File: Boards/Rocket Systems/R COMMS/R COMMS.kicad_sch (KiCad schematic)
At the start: 67 parts, among them IC1 NSVT30010MXV6T1G, IC2 NSVT30010MXV6T1G, J2 22285061, J4 MEM2061-01-188-00-A_REVA, J5 SMA_CONNECTOR, J6 SMA_CONNECTOR, J7 SMA_CONNECTOR, J8 1190297, SW1 D2F-01-D, U3 SX1280IMLTRT, U4 NRF21540-QDAA-R, U6 MAX485CSA+T, U7 MCP9808T-E/MC, U9 CD-PA1616

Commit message: Update R Comms board
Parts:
- R15, R17: value 10K -> 10k
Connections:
- net +3.3V: now also R15.1; no longer R15.2
- net NRF21540 SPI ~{CS}: no longer IC2.2 (B2)
- net RS_ENABLE: now also IC2.5 (B1)
- net SX1280 SPI ~{CS}: no longer IC2.5 (B1)
- net TEMP ALERT: now also IC2.2 (B2)
- net GPS I2C SCL renamed SDL I2C
- net GPS I2C SDA renamed SDA I2C
- net SDA I2C: now also R15.2; no longer R15.1
- net GPS UART RX: no longer names the net of U9.10 (RX0)
- net GPS UART TX: no longer names the net of U9.9 (TX0)
- no-connect marks 4 -> 6
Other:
- sheet RP2040 ports: added GP13/SPI1 ~{CS}, GPIO12; removed GP12/I2C0 SDA, GP13/I2C0 SCL
- note added: "I2C for GPS & Temp Sensor"
- moved on the sheet: CR3, CR5, CR6, IC2, J2, R22, R25

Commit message: Communication boards update
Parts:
- removed J2: 22285061, CONN Male Header:CONN_SD-42375-001_M320_06_MOL, symbol 2025-01-27_18-08-00:22285061
- added J2: 22022065, CONN_SA-4455_06_TE_MOL, symbol CONN_SA-4455_06_TE_MOL:22022065
- U3: footprint SX1280:QFN24_4X4_SEM -> QFN24_4X4_SEM
- U4: footprint RF FEM:QFN16_4X4_NOR -> QFN16_4X4_NOR
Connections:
- net NRF21540 SPI MISO is gone; now on net RADIO SPI MISO: U4.14 (MISO)
- net NRF21540 SPI MOSI is gone; now on net RADIO SPI MOSI: U4.13 (MOSI)
- net NRF21540 SPI SCK is gone; now on net RADIO SPI SCK: U4.12 (SCK)
- net SX1280 SPI MISO is gone; now on net RADIO SPI MISO: U3.16 (MISO_TX)
- net SX1280 SPI MOSI is gone; now on net RADIO SPI MOSI: U3.17 (MOSI_RX)
- net SX1280 SPI SCK is gone; now on net RADIO SPI SCK: U3.18 (SCK_RTSN)
- net TEMP SDA I2C is gone; now on net SDA I2C: R21.2, U7.1 (SDA)
- net TEMP SDL I2C is gone; now on net SDL I2C: R20.2, U7.2 (SCL)
- net GND: now also J2.6
- net OBC UART CTS: now also J2.4
- net OBC UART RTS: now also J2.5
- net OBC UART RX: now also J2.3
- net OBC UART TX: now also J2.2
- net V_IN: now also J2.1
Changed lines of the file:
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@@
 		)
 	)
-	(label "NRF21540 SPI MISO"
+	(label "RADIO SPI MISO"
 		(at 218.44 238.76 0)
 		(effects
@@
 		)
 	)
-	(label "NRF21540 SPI SCK"
+	(label "RADIO SPI SCK"
 		(at 218.44 233.68 0)
 		(effects
@@
 		)
 	)
-	(label "SX1280 SPI SCK"
+	(label "RADIO SPI SCK"
 		(at 168.91 236.22 180)
 		(effects
@@
 		)
 	)
-	(label "NRF21540 SPI MOSI"
+	(label "RADIO SPI MOSI"
 		(at 218.44 236.22 0)
 		(effects
@@
 		)
 	)
-	(label "TEMP SDA I2C"
+	(label "SDA I2C"
 		(at 21.59 154.305 0)
 		(effects
@@
 		)
 	)
-	(label "TEMP SDL I2C"
+	(label "SDL I2C"
 		(at 21.59 156.845 0)
 		(effects
@@
 		)
 	)
-	(label "SX1280 SPI MISO"
+	(label "RADIO SPI MISO"
 		(at 168.91 241.3 180)
 		(effects
@@
 		)
 	)
-	(label "SX1280 SPI MOSI"
+	(label "RADIO SPI MOSI"
 		(at 168.91 238.76 180)
 		(effects
@@
 	)
 	(symbol
-		(lib_id "2025-01-27_18-08-00:22285061")
-		(at 33.655 58.42 180)
-		(unit 1)
-		(exclude_from_sim no)
-		(in_bom yes)
-		(on_board yes)
-		(dnp no)
-		(fields_autoplaced yes)
-		(property "Reference" "J2"
-			(at 24.765 38.1 0)
-			(effects
-				(font
-					(size 1.524 1.524)
-				)
-			)
-		)
-		(property "Value" "22285061"
-			(at 24.765 40.64 0)
-			(effects
-				(font
-					(size 1.524 1.524)
-				)
-			)
-		)
-		(property "Footprint" "CONN Male Header:CONN_SD-42375-001_M320_06_MOL"
-			(at 33.655 58.42 0)
-			(effects
-				(font
-					(size 1.27 1.27)
-					(italic yes)
-				)
-				(hide yes)
-			)
-		)
-		(property "Datasheet" "22285061"
-			(at 33.655 58.42 0)
-			(effects
-				(font
-					(size 1.27 1.27)
-					(italic yes)
-				)
-				(hide yes)
-			)
-		)
-		(property "Description" ""
-			(at 33.655 58.42 0)
-			(effects
-				(font
-					(size 1.27 1.27)
-				)
-				(hide yes)
-			)
-		)
-		(pin "6"
-		)
-		(pin "3"
-		)
-		(pin "4"
-		)
-		(pin "1"
-		)
-		(pin "5"
-		)
-		(pin "2"
-		)
-		(instances
-			(project ""
-				(path "/169b1789-9bea-4709-830d-1c7983087293"
-					(reference "J2")
-					(unit 1)
-				)
-			)
-		)
-	)
-	(symbol
 		(lib_id "1190297:1190297")
 		(at 359.41 146.05 90)
@@
 	)
 	(symbol
+		(lib_id "CONN_SA-4455_06_TE_MOL:22022065")
+		(at 33.655 45.72 0)
+		(mirror y)
+		(unit 1)
+		(exclude_from_sim no)
+		(in_bom yes)
+		(on_board yes)
+		(dnp no)
+		(property "Reference" "J2"
+			(at 19.685 50.7999 0)
+			(effects
+				(font
+					(size 1.524 1.524)
+				)
+				(justify left)
+			)
+		)
+		(property "Value" "22022065"
+			(at 19.685 53.3399 0)
+			(effects
+				(font
+					(size 1.524 1.524)
+				)
+				(justify left)
+			)
+		)
+		(property "Footprint" "CONN_SA-4455_06_TE_MOL"
+			(at 33.655 41.91 0)
+			(effects
+				(font
+					(size 1.27 1.27)
+					(italic yes)
+				)
+				(hide yes)
+			)
+		)
+		(property "Datasheet" "22022065"
+			(at 33.655 40.132 0)
+			(effects
+				(font
+					(size 1.27 1.27)
+					(italic yes)
+				)
+				(hide yes)
+			)
+		)
+		(property "Description" ""
+			(at 33.655 45.72 0)
+			(effects
+				(font
+					(size 1.27 1.27)
+				)
+				(hide yes)
+			)
+		)
+		(pin "1"
+		)
+		(pin "6"
+		)
+		(pin "2"
+		)
+		(pin "5"
+		)
+		(pin "3"
+		)
+		(pin "4"
+		)
+		(instances
+			(project ""
+				(path "/169b1789-9bea-4709-830d-1c7983087293"
+					(reference "J2")
+					(unit 1)
+				)
+			)
+		)
+	)
+	(symbol
 		(lib_id "power:+3.3V")
 		(at 288.29 139.7 0)
@@
 			)
 		)
-		(property "Footprint" "SX1280:QFN24_4X4_SEM"
+		(property "Footprint" "QFN24_4X4_SEM"
 			(at 93.98 218.44 0)
 			(effects
@@
 			)
 		)
-		(property "Footprint" "RF FEM:QFN16_4X4_NOR"
+		(property "Footprint" "QFN16_4X4_NOR"
 			(at 260.858 203.454 0)
 			(effects

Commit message: System update
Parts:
- removed J8: 1190297, 1190297, symbol 1190297:1190297
- added J9: Conn_01x04_Socket, symbol Connector:Conn_01x04_Socket
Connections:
- net +5V: now also J9.1 (Pin_1)
- net GND: now also J9.4 (Pin_4)
- net RS_A: now reaches R26.2, R27.2, U6.6 (A)
- net RS_A: now also J9.3 (Pin_3)
- net RS_B: now reaches R26.1, R28.1, U6.7 (B)
- net RS_B: now also J9.2 (Pin_2)
- net V_IN renamed OBC 5V
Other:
- moved on the sheet: C1, J2, J4

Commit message: USB-C PD update and schematic corrections
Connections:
- net OBC 5V is gone; now on net +5V: J2.1
- net OBC UART RX: now also J2.2; no longer J2.3
- net OBC UART TX: now also J2.3; no longer J2.2
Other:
- sheet RP2040 ports: added none; removed +5V
- note added: "SPI must be limited to 5MHz"
- moved on the sheet: J9

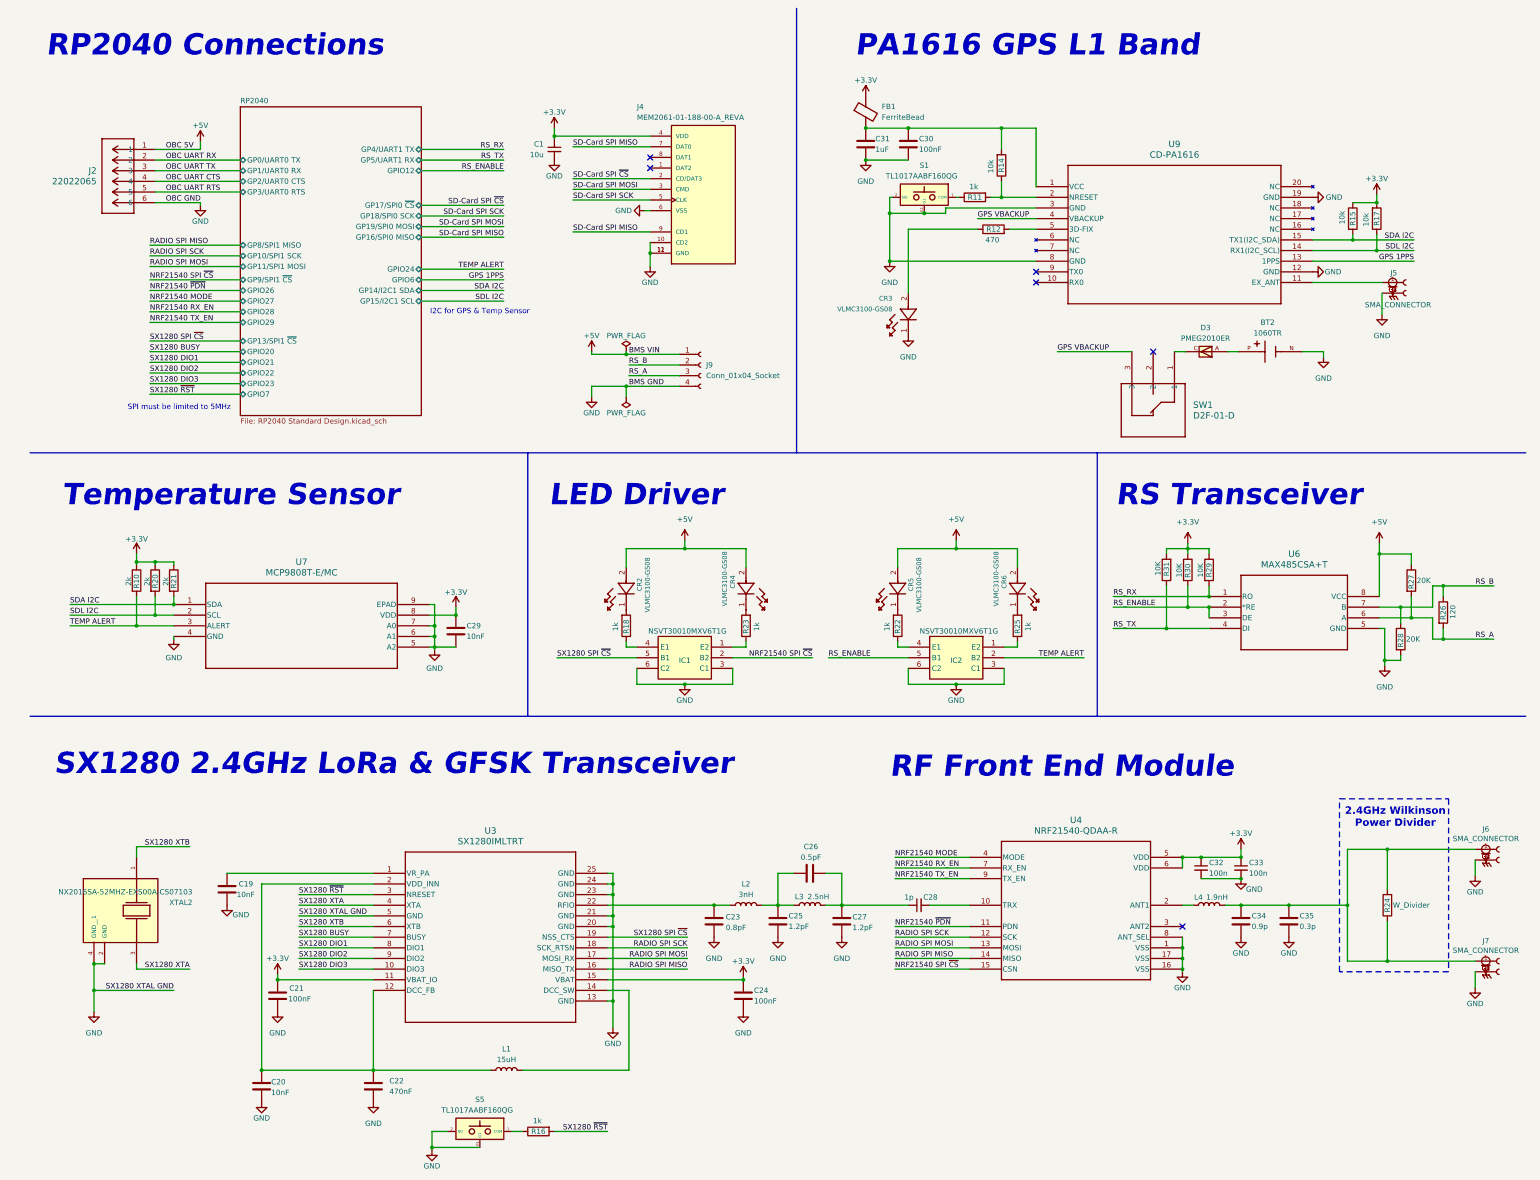
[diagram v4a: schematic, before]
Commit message: Current sensor update implementation and 8.4V DC.DC implementation
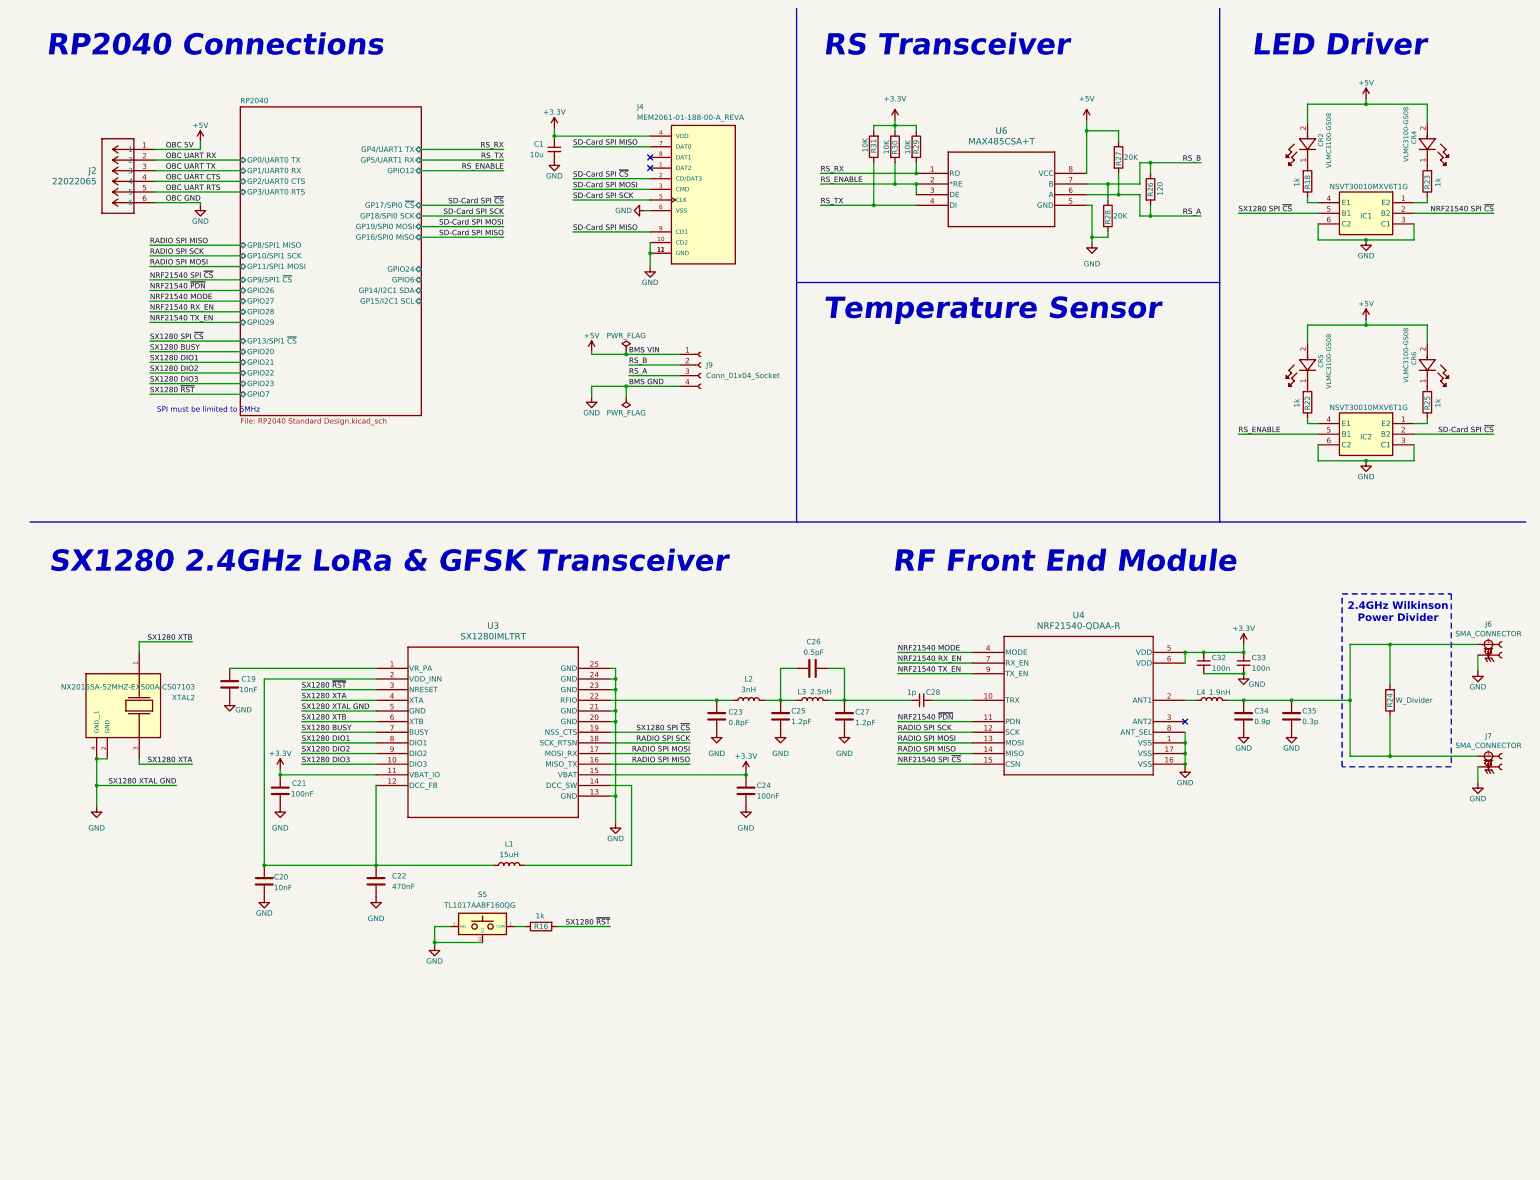
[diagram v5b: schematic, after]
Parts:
- removed BT2: 1060TR, BAT Holder 1060TR:BAT_1060TR, symbol 1060TR:1060TR
- removed C29: 10nF, Capacitor-0402:Capacitor_0402, symbol Device:C
- removed C30: 100nF, Capacitor-0402:Capacitor_0402, symbol Device:C
- removed C31: 1uF, Capacitor-0402:Capacitor_0402, symbol Device:C
- removed CR3: VLMC3100-GS08, LED-Green_VLMC3100-GS08:LED_PLCC_VSMB, symbol GreenLED__VLMC3100-GS08:VLMC3100-GS08
- removed D3: PMEG2010ER, Diode-Schottky_PMEG2010ER:SODFL3517X110N, symbol PMEG2010ER:PMEG2010ER
- removed FB1: FerriteBead, Ferrite:Ferrite_0603, symbol Device:FerriteBead
- removed J5: SMA_CONNECTOR, SMA_CONNECTOR:LPRS_SMA_CONNECTOR, symbol SMA_CONNECTOR:SMA_CONNECTOR
- removed R10, R20, R21: 2k, Resistor-0402:RES_0402, symbol Device:R
- removed R11: 1k, Resistor-0402:RES_0402, symbol Device:R
- removed R12: 470, Resistor-0402:RES_0402, symbol Device:R
- removed R14, R15, R17: 10k, Resistor-0402:RES_0402, symbol Device:R
- removed S1: TL1017AABF160QG, TL1017AABF160QG, symbol TL1017AABF160QG:TL1017AABF160QG
- removed SW1: D2F-01-D, Switch D2F-01:D2F-01-D_OMR, symbol Switch_D2F-01:D2F-01-D
- removed U7: MCP9808T-E/MC, MCP9808-TempSensor:DFN8_2x3MC_MCH, symbol MCP9808:MCP9808T-E_MC
- removed U9: CD-PA1616, GPS_adafruit:CD-PA1616D_ADA, symbol GPS_adafruit:5186
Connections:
- net TEMP ALERT is gone; now on net SD-Card SPI ~{CS}: IC2.2 (B2)
- no-connect marks 6 -> 3
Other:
- note removed: "I2C for GPS & Temp Sensor"
- note removed: "PA1616 GPS L1 Band"
- moved on the sheet: C19, C20, C21, C22, C23, C24, C25, C26, C27, C28, C32, C33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

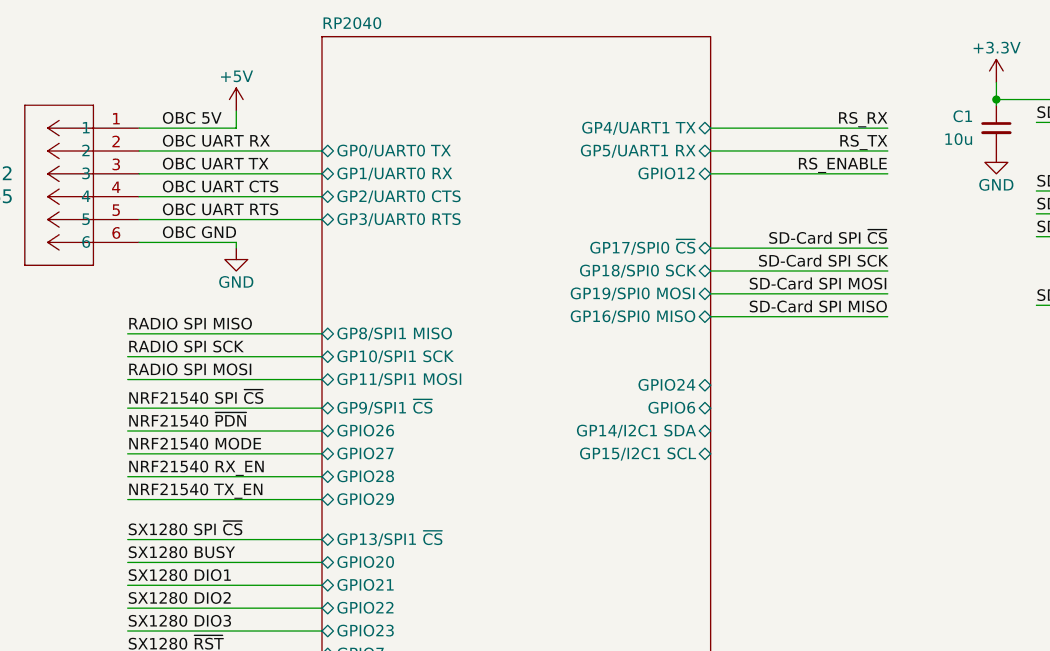
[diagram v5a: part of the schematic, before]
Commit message: TVCS pinout rework
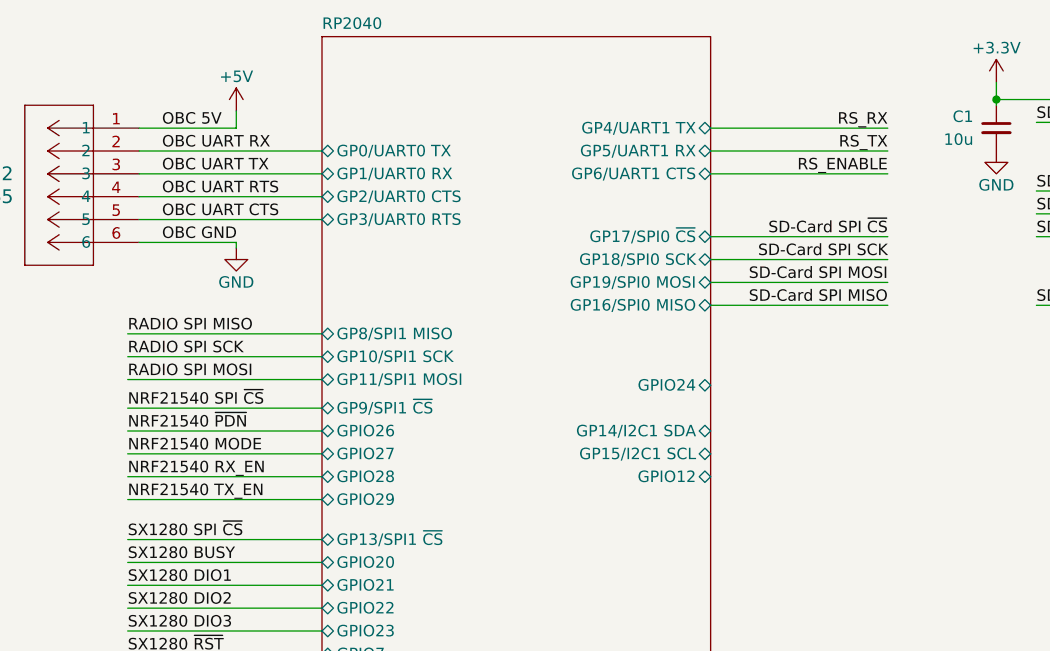
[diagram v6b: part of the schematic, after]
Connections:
- net OBC UART CTS: now also J2.5; no longer J2.4
- net OBC UART RTS: now also J2.4; no longer J2.5
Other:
- sheet RP2040 ports: added GP6/UART1 CTS; removed GPIO6
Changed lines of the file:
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@@
 	(wire
 		(pts
-			(xy 105.41 50.8) (xy 125.095 50.8)
-		)
-		(stroke
-			(width 0)
-			(type default)
-		)
-	)
-	(wire
-		(pts
 			(xy 269.24 53.975) (xy 269.24 57.785)
 		)
@@
 	(wire
 		(pts
-			(xy 105.41 61.595) (xy 125.095 61.595)
+			(xy 105.41 60.325) (xy 125.095 60.325)
 		)
 		(stroke
@@
 	(wire
 		(pts
-			(xy 105.41 59.055) (xy 125.095 59.055)
+			(xy 105.41 57.785) (xy 125.095 57.785)
 		)
 		(stroke
@@
 	(wire
 		(pts
-			(xy 105.41 66.675) (xy 125.095 66.675)
+			(xy 105.41 65.405) (xy 125.095 65.405)
 		)
 		(stroke
@@
 	(wire
 		(pts
+			(xy 105.41 50.8) (xy 125.095 50.8)
+		)
+		(stroke
+			(width 0)
+			(type default)
+		)
+	)
+	(wire
+		(pts
 			(xy 141.605 55.245) (xy 160.02 55.245)
 		)
@@
 	(wire
 		(pts
-			(xy 105.41 64.135) (xy 125.095 64.135)
+			(xy 105.41 62.865) (xy 125.095 62.865)
 		)
 		(stroke
@@
 		)
 	)
-	(label "OBC UART RTS"
-		(at 44.45 55.88 0)
-		(effects
-			(font
-				(size 1.27 1.27)
-			)
-			(justify left bottom)
-		)
-	)
 	(label "SX1280 XTA"
 		(at 50.8 192.405 180)
@@
 	)
 	(label "SD-Card SPI SCK"
-		(at 125.095 61.595 180)
+		(at 125.095 60.325 180)
 		(effects
 			(font
@@
 	)
 	(label "SD-Card SPI MISO"
-		(at 125.095 66.675 180)
+		(at 125.095 65.405 180)
 		(effects
 			(font
@@
 	)
 	(label "OBC UART CTS"
+		(at 44.45 55.88 0)
+		(effects
+			(font
+				(size 1.27 1.27)
+			)
+			(justify left bottom)
+		)
+	)
+	(label "OBC UART RTS"
 		(at 44.45 53.34 0)
 		(effects
@@
 	)
 	(label "SD-Card SPI ~{CS}"
-		(at 125.095 59.055 180)
+		(at 125.095 57.785 180)
 		(effects
 			(font
@@
 	)
 	(label "SD-Card SPI MOSI"
-		(at 125.095 64.135 180)
+		(at 125.095 62.865 180)
 		(effects
 			(font
@@
 		)
 		(pin "GP19{slash}SPI0 MOSI" bidirectional
-			(at 105.41 64.135 0)
+			(at 105.41 62.865 0)
 			(effects
 				(font
@@
 		)
 		(pin "GP17{slash}SPI0 ~{CS}" bidirectional
-			(at 105.41 59.055 0)
+			(at 105.41 57.785 0)
 			(effects
 				(font
@@
 		)
 		(pin "GP18{slash}SPI0 SCK" bidirectional
-			(at 105.41 61.595 0)
+			(at 105.41 60.325 0)
 			(effects
 				(font
@@
 			)
 		)
-		(pin "GPIO6" bidirectional
-			(at 105.41 76.835 0)
+		(pin "GP6{slash}UART1 CTS" bidirectional
+			(at 105.41 50.8 0)
 			(effects
 				(font
@@
 		)
 		(pin "GPIO12" bidirectional
-			(at 105.41 50.8 0)
+			(at 105.41 84.455 0)
 			(effects
 				(font
@@
 		)
 		(pin "GP16{slash}SPI0 MISO" bidirectional
-			(at 105.41 66.675 0)
+			(at 105.41 65.405 0)
 			(effects
 				(font
